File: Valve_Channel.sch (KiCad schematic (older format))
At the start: 12 parts, among them Q1 MMBT3904, Q2 Q_PMOS_GDS, U9 INA181AX

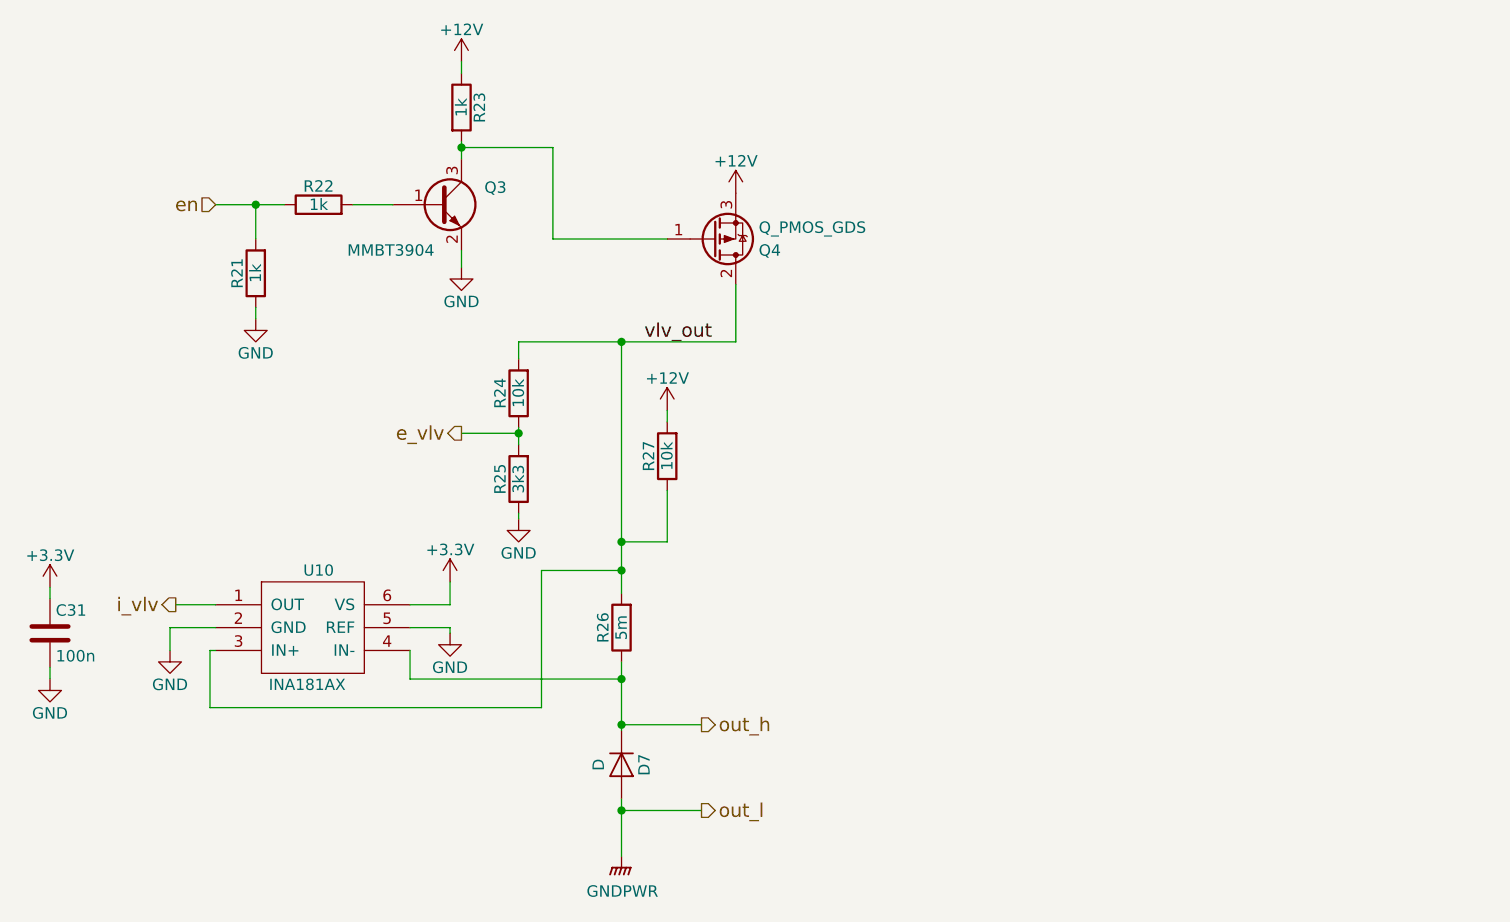
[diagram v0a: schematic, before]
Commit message: added bldc channel
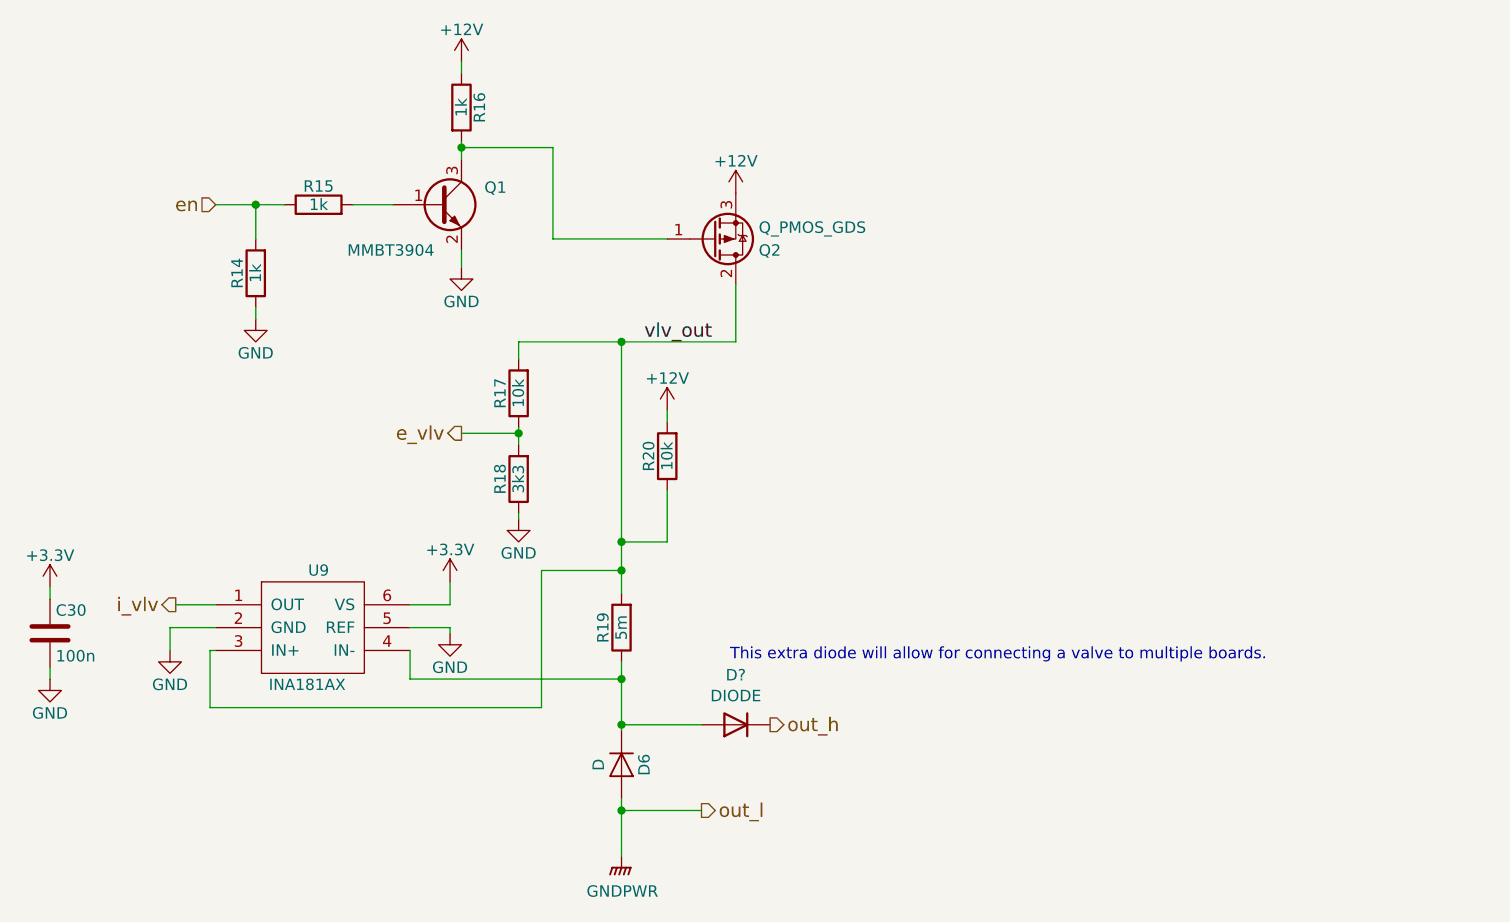
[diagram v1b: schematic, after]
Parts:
- added D?: DIODE, symbol Simulation_SPICE:DIODE
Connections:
- net out_h: now also D?.2 (K); no longer D6.1 (K), R19.1, U9.4 (IN-)
- new net: D6.1 (K), D?.1 (A), R19.1, U9.4 (IN-)
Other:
- note added: "This extra diode will allow for connecting a valve to multiple boards.\n"
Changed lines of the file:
@@
 $Descr A4 11693 8268
 encoding utf-8
-Sheet 11 12
+Sheet 8 14
 Title "Engine Controller Series 3"
 Date ""
@@
 AR Path="/5E63996E/5E506090/596707F4" Ref="#PWR?"  Part="1"
 AR Path="/5E63996E/5E506A1D/596707F4" Ref="#PWR?"  Part="1"
-F 0 "#PWR085" H 6575 2525 50  0001 C CNN
+F 0 "#PWR073" H 6575 2525 50  0001 C CNN
 F 1 "+12V" H 6575 2815 50  0000 C CNN
 F 2 "" H 6575 2675 50  0001 C CNN
@@
 AR Path="/5E63996E/5E506090/596711AE" Ref="#PWR?"  Part="1"
 AR Path="/5E63996E/5E506A1D/596711AE" Ref="#PWR?"  Part="1"
-F 0 "#PWR084" H 6275 3475 50  0001 C CNN
+F 0 "#PWR072" H 6275 3475 50  0001 C CNN
 F 1 "+12V" H 6275 3765 50  0000 C CNN
 F 2 "" H 6275 3625 50  0001 C CNN
@@
 AR Path="/5E63996E/5E506090/59671CF5" Ref="#PWR?"  Part="1"
 AR Path="/5E63996E/5E506A1D/59671CF5" Ref="#PWR?"  Part="1"
-F 0 "#PWR081" H 5375 2750 50  0001 C CNN
+F 0 "#PWR069" H 5375 2750 50  0001 C CNN
 F 1 "GND" H 5375 2850 50  0000 C CNN
 F 2 "" H 5375 3000 50  0001 C CNN
@@
 AR Path="/5E63996E/5E506090/596722EC" Ref="#PWR?"  Part="1"
 AR Path="/5E63996E/5E506A1D/596722EC" Ref="#PWR?"  Part="1"
-F 0 "#PWR082" H 5625 3850 50  0001 C CNN
+F 0 "#PWR070" H 5625 3850 50  0001 C CNN
 F 1 "GND" H 5625 3950 50  0000 C CNN
 F 2 "" H 5625 4100 50  0001 C CNN
@@
 AR Path="/5E63996E/5E506090/59672E62" Ref="R?"  Part="1"
 AR Path="/5E63996E/5E506A1D/59672E62" Ref="R?"  Part="1"
-F 0 "R24" V 5705 3550 50  0000 C CNN
+F 0 "R17" V 5705 3550 50  0000 C CNN
 F 1 "10k" V 5625 3550 50  0000 C CNN
 F 2 "Resistors_SMD:R_0603" V 5555 3550 50  0001 C CNN
@@
 AR Path="/5E63996E/5E506090/59672F15" Ref="R?"  Part="1"
 AR Path="/5E63996E/5E506A1D/59672F15" Ref="R?"  Part="1"
-F 0 "R25" V 5705 3925 50  0000 C CNN
+F 0 "R18" V 5705 3925 50  0000 C CNN
 F 1 "3k3" V 5625 3925 50  0000 C CNN
 F 2 "Resistors_SMD:R_0603" V 5555 3925 50  0001 C CNN
@@
 AR Path="/5E63996E/5E506090/59672F5E" Ref="R?"  Part="1"
 AR Path="/5E63996E/5E506A1D/59672F5E" Ref="R?"  Part="1"
-F 0 "R27" V 6355 3825 50  0000 C CNN
+F 0 "R20" V 6355 3825 50  0000 C CNN
 F 1 "10k" V 6275 3825 50  0000 C CNN
 F 2 "Resistors_SMD:R_0603" V 6205 3825 50  0001 C CNN
@@
 AR Path="/5E63996E/5E506090/59672FA2" Ref="R?"  Part="1"
 AR Path="/5E63996E/5E506A1D/59672FA2" Ref="R?"  Part="1"
-F 0 "R21" V 4555 3025 50  0000 C CNN
+F 0 "R14" V 4555 3025 50  0000 C CNN
 F 1 "1k" V 4475 3025 50  0000 C CNN
 F 2 "Resistors_SMD:R_0603" V 4405 3025 50  0001 C CNN
@@
 AR Path="/5E63996E/5E506090/59673012" Ref="R?"  Part="1"
 AR Path="/5E63996E/5E506A1D/59673012" Ref="R?"  Part="1"
-F 0 "R22" V 4830 2725 50  0000 C CNN
+F 0 "R15" V 4830 2725 50  0000 C CNN
 F 1 "1k" V 4750 2725 50  0000 C CNN
 F 2 "Resistors_SMD:R_0603" V 4680 2725 50  0001 C CNN
@@
 AR Path="/5E63996E/5E506090/5967307F" Ref="R?"  Part="1"
 AR Path="/5E63996E/5E506A1D/5967307F" Ref="R?"  Part="1"
-F 0 "R26" V 6155 4575 50  0000 C CNN
+F 0 "R19" V 6155 4575 50  0000 C CNN
 F 1 "5m" V 6075 4575 50  0000 C CNN
 F 2 "Resistors_SMD:R_1206" V 6005 4575 50  0001 C CNN
@@
 AR Path="/5E63996E/5E506090/59673A80" Ref="Q?"  Part="1"
 AR Path="/5E63996E/5E506A1D/59673A80" Ref="Q?"  Part="1"
-F 0 "Q3" H 5475 2800 50  0000 L CNN
+F 0 "Q1" H 5475 2800 50  0000 L CNN
 F 1 "MMBT3904" H 4875 2525 50  0000 L CNN
 F 2 "TO_SOT_Packages_SMD:SOT-23" H 5475 2650 50  0001 L CIN
@@
 AR Path="/5E63996E/5E506090/59673D60" Ref="R?"  Part="1"
 AR Path="/5E63996E/5E506A1D/59673D60" Ref="R?"  Part="1"
-F 0 "R23" V 5455 2300 50  0000 C CNN
+F 0 "R16" V 5455 2300 50  0000 C CNN
 F 1 "1k" V 5375 2300 50  0000 C CNN
 F 2 "Resistors_SMD:R_0603" V 5305 2300 50  0001 C CNN
@@
 AR Path="/5E63996E/5E506090/59673EA8" Ref="#PWR?"  Part="1"
 AR Path="/5E63996E/5E506A1D/59673EA8" Ref="#PWR?"  Part="1"
-F 0 "#PWR077" H 4475 2975 50  0001 C CNN
+F 0 "#PWR065" H 4475 2975 50  0001 C CNN
 F 1 "GND" H 4475 3075 50  0000 C CNN
 F 2 "" H 4475 3225 50  0001 C CNN
@@
 AR Path="/5E63996E/5E506090/59674072" Ref="#PWR?"  Part="1"
 AR Path="/5E63996E/5E506A1D/59674072" Ref="#PWR?"  Part="1"
-F 0 "#PWR080" H 5375 1950 50  0001 C CNN
+F 0 "#PWR068" H 5375 1950 50  0001 C CNN
 F 1 "+12V" H 5375 2240 50  0000 C CNN
 F 2 "" H 5375 2100 50  0001 C CNN
@@
 AR Path="/5E63996E/5E506090/59699268" Ref="U?"  Part="1"
 AR Path="/5E63996E/5E506A1D/59699268" Ref="U?"  Part="1"
-F 0 "U10" H 4750 4825 49  0000 C CNN
+F 0 "U9" H 4750 4825 49  0000 C CNN
 F 1 "INA181AX" H 4700 4325 49  0000 C CNN
 F 2 "TO_SOT_Packages_SMD:SOT-23-6" H 4300 4875 49  0001 C CNN
@@
 AR Path="/5E63996E/5E506090/59699513" Ref="#PWR?"  Part="1"
 AR Path="/5E63996E/5E506A1D/59699513" Ref="#PWR?"  Part="1"
-F 0 "#PWR076" H 4100 4425 50  0001 C CNN
+F 0 "#PWR064" H 4100 4425 50  0001 C CNN
 F 1 "GND" H 4100 4525 50  0000 C CNN
 F 2 "" H 4100 4675 50  0001 C CNN
@@
 AR Path="/5E63996E/5E506090/59699670" Ref="#PWR?"  Part="1"
 AR Path="/5E63996E/5E506A1D/59699670" Ref="#PWR?"  Part="1"
-F 0 "#PWR078" H 5325 4225 50  0001 C CNN
+F 0 "#PWR066" H 5325 4225 50  0001 C CNN
 F 1 "+3.3V" H 5325 4515 50  0000 C CNN
 F 2 "" H 5325 4375 50  0001 C CNN
@@
 AR Path="/5E63996E/5E506090/597621D1" Ref="C?"  Part="1"
 AR Path="/5E63996E/5E506A1D/597621D1" Ref="C?"  Part="1"
-F 0 "C31" H 3600 4700 50  0000 L CNN
+F 0 "C30" H 3600 4700 50  0000 L CNN
 F 1 "100n" H 3600 4500 50  0000 L CNN
 F 2 "Capacitors_SMD:C_0603" H 3613 4450 50  0001 C CNN
@@
 AR Path="/5E63996E/5E506090/59730D47" Ref="D?"  Part="1"
 AR Path="/5E63996E/5E506A1D/59730D47" Ref="D?"  Part="1"
-F 0 "D7" H 6075 5275 50  0000 C CNN
+F 0 "D6" H 6075 5275 50  0000 C CNN
 F 1 "D" H 6075 5075 50  0000 C CNN
 F 2 "sternie:SOD-128" H 6075 5175 50  0001 C CNN
@@
 AR Path="/5E63996E/5E506090/5A0B2DB5" Ref="#PWR?"  Part="1"
 AR Path="/5E63996E/5E506A1D/5A0B2DB5" Ref="#PWR?"  Part="1"
-F 0 "#PWR074" H 3575 4250 50  0001 C CNN
+F 0 "#PWR062" H 3575 4250 50  0001 C CNN
 F 1 "+3.3V" H 3575 4540 50  0000 C CNN
 F 2 "" H 3575 4400 50  0001 C CNN
@@
 AR Path="/5E63996E/5E506090/5A0B2DE7" Ref="#PWR?"  Part="1"
 AR Path="/5E63996E/5E506A1D/5A0B2DE7" Ref="#PWR?"  Part="1"
-F 0 "#PWR075" H 3575 4550 50  0001 C CNN
+F 0 "#PWR063" H 3575 4550 50  0001 C CNN
 F 1 "GND" H 3575 4650 50  0000 C CNN
 F 2 "" H 3575 4800 50  0001 C CNN
@@
 AR Path="/5E63996E/5E506090/59699546" Ref="#PWR?"  Part="1"
 AR Path="/5E63996E/5E506A1D/59699546" Ref="#PWR?"  Part="1"
-F 0 "#PWR079" H 5325 4350 50  0001 C CNN
+F 0 "#PWR067" H 5325 4350 50  0001 C CNN
 F 1 "GND" H 5325 4450 50  0000 C CNN
 F 2 "" H 5325 4600 50  0001 C CNN
@@
 Wire Wire Line
 	5325 4475 5325 4375
-Text HLabel 6425 5000 2    60   Output ~ 0
+Text HLabel 6725 5000 2    60   Output ~ 0
 out_h
 Text HLabel 6425 5375 2    60   Output ~ 0
@@
 AR Path="/5E63996E/5E506090/5A1E0B4E" Ref="Q?"  Part="1"
 AR Path="/5E63996E/5E506A1D/5A1E0B4E" Ref="Q?"  Part="1"
-F 0 "Q4" H 6675 2925 50  0000 L CNN
+F 0 "Q2" H 6675 2925 50  0000 L CNN
 F 1 "Q_PMOS_GDS" H 6675 2825 50  0000 L CNN
 F 2 "TO_SOT_Packages_SMD:TO-252-2" H 6675 2975 50  0001 C CNN
@@
 AR Path="/5E63996E/5E506090/5C0A5B78" Ref="#PWR?"  Part="1"
 AR Path="/5E63996E/5E506A1D/5C0A5B78" Ref="#PWR?"  Part="1"
-F 0 "#PWR083" H 6075 5375 50  0001 C CNN
+F 0 "#PWR071" H 6075 5375 50  0001 C CNN
 F 1 "GNDPWR" H 6079 5421 50  0000 C CNN
 F 2 "" H 6075 5525 50  0001 C CNN
@@
 	1    0    0    -1
 $EndComp
+$Comp
+L Simulation_SPICE:DIODE D?
+U 1 1 5E892DE8
+P 6575 5000
+F 0 "D?" H 6575 5217 50  0000 C CNN
+F 1 "DIODE" H 6575 5126 50  0000 C CNN
+F 2 "" H 6575 5000 50  0001 C CNN
+F 3 "~" H 6575 5000 50  0001 C CNN
+F 4 "Y" H 6575 5000 50  0001 L CNN "Spice_Netlist_Enabled"
+F 5 "V" H 6575 5000 50  0001 L CNN "Spice_Primitive"
+	1    6575 5000
+	1    0    0    -1
+$EndComp
+Text Notes 6550 4725 0    50   ~ 0
+This extra diode will allow for connecting a valve to multiple boards.\n
 $EndSCHEMATC
